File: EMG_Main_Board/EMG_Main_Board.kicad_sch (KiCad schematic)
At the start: 14 parts, among them IC1 EFR32BG13P732F512GM48-D, IC2 LD1117DT18TR, J1 ADC input, J2 USB_C_Receptacle, J3 UART, J4 UART, J5 1.8V, J6 Conn_01x02_Pin, U1 LD1117S33TR_SOT223, U3 STM32G0B1RET6

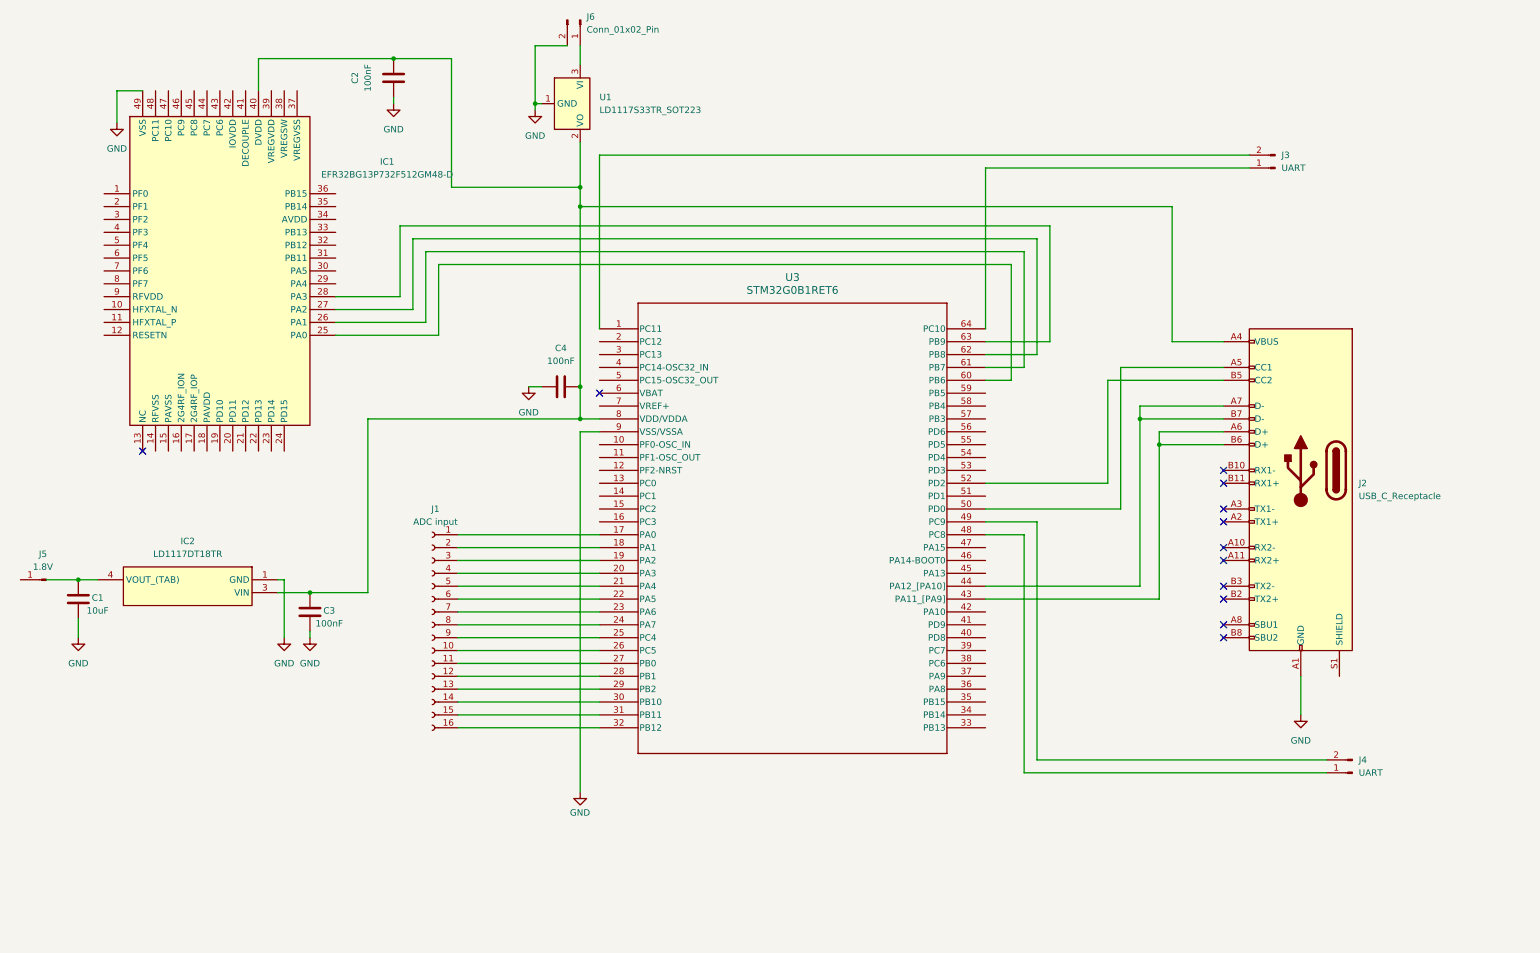
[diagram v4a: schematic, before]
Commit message: add 38.4 and 48MHz crystals for BLE and MCU, resp.
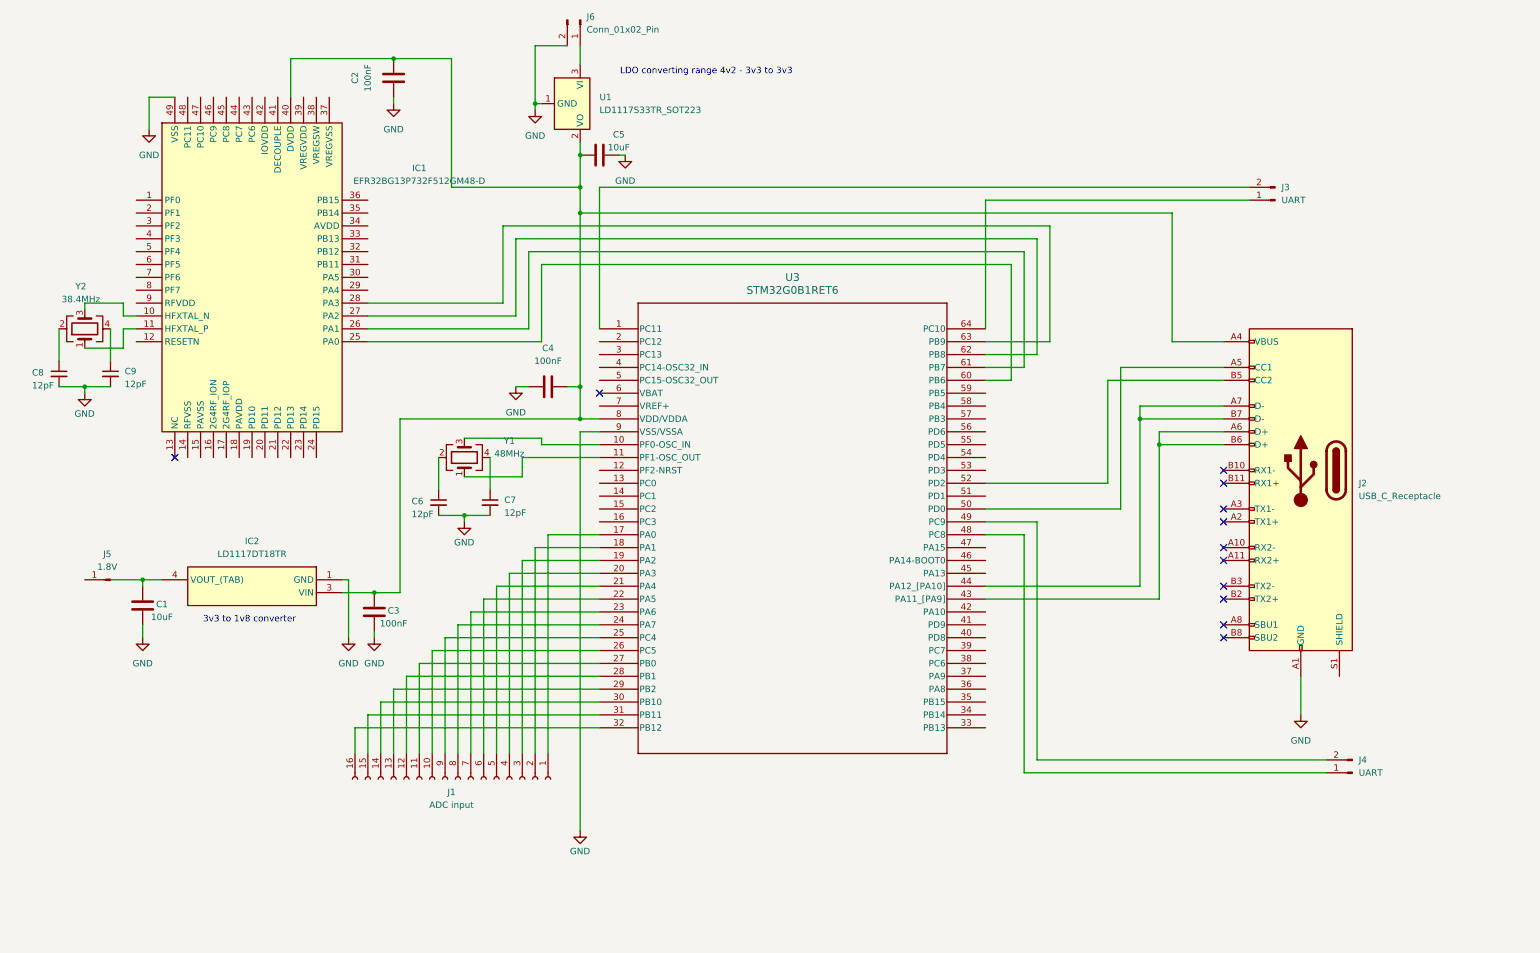
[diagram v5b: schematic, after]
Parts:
- added C5: 10uF, symbol Device:C
- added C6, C7, C8, C9: 12pF, symbol Device:C_Small
- added Y1: 48MHz, symbol Device:Crystal_GND24
- added Y2: 38.4MHz, symbol Device:Crystal_GND24
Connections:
- net GND: now also C5.2, C6.2, C7.2, C8.2, C9.2
- net at C2.1, C3.1, C4.1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: now also C5.1
- net at IC1.10 (HFXTAL_N): now also Y2.3
- net at IC1.11 (HFXTAL_P): now also Y2.1
- net at U3.10 (PF0-OSC_IN): now also Y1.3
- net at U3.11 (PF1-OSC_OUT): now also Y1.1
- new net: C6.1, Y1.2
- new net: C7.1, Y1.4
- new net: C9.1, Y2.4
- new net: C8.1, Y2.2
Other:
- note added: "3v3 to 1v8 converter"
- note added: "LDO converting range 4v2 - 3v3 to 3v3"
- moved on the sheet: C1, C3, C4, IC1, IC2, J1, J3, J5

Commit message: add ON/OFF slide switch and RST button to sch
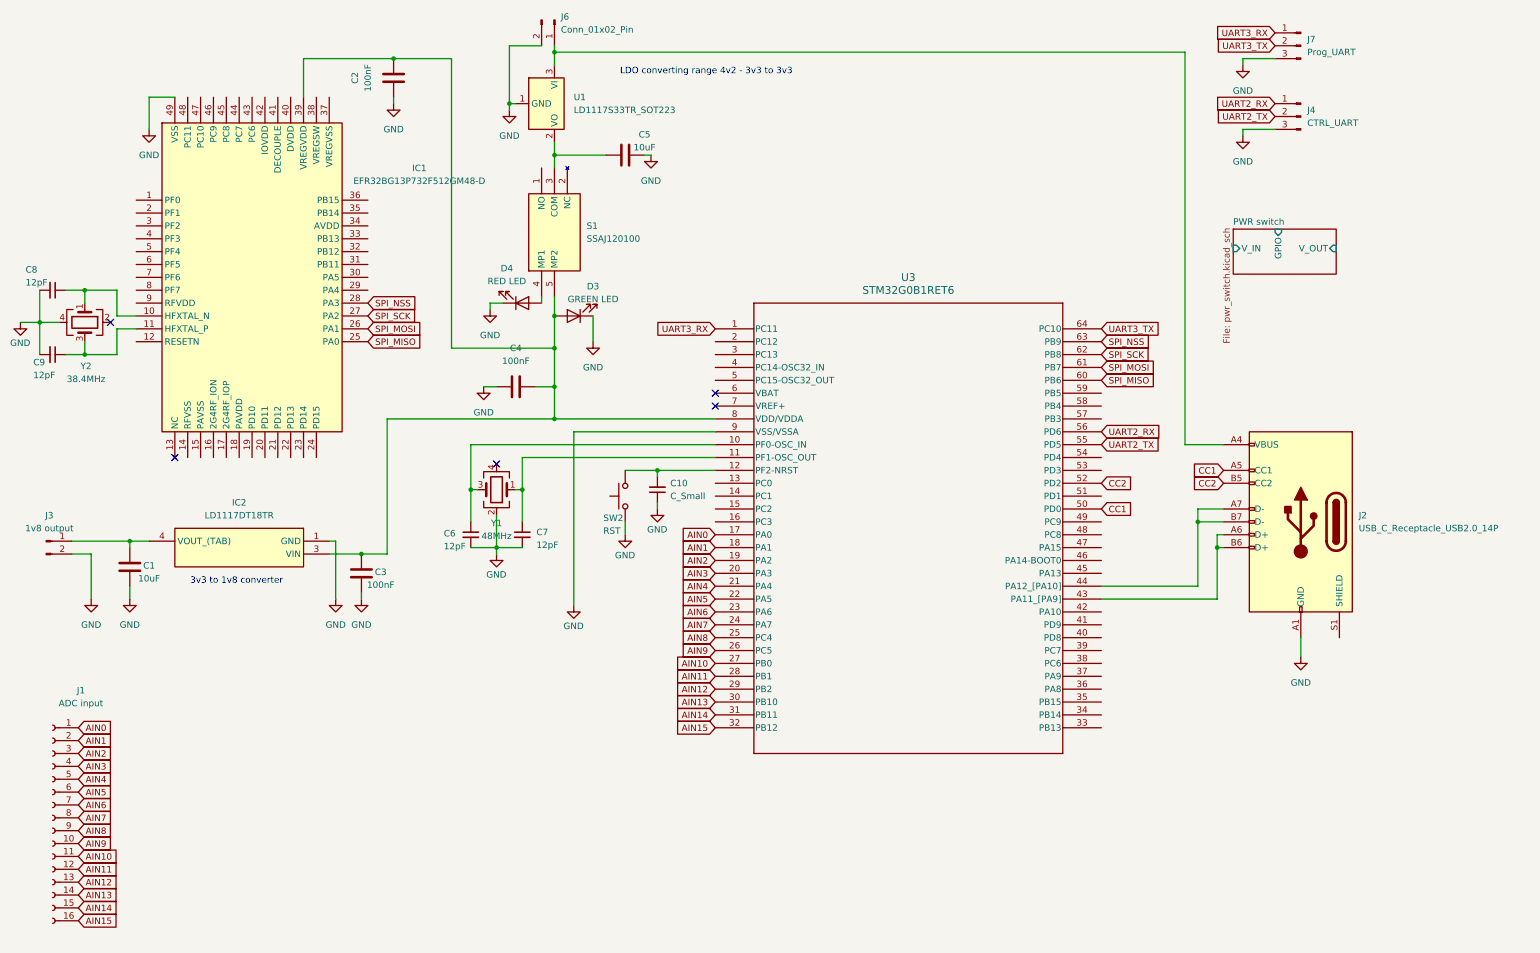
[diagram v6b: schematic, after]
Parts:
- removed J2: USB_C_Receptacle, symbol Connector:USB_C_Receptacle
- removed J4: UART, symbol Connector:Conn_01x02_Pin
- removed J5: 1.8V, symbol Connector:Conn_01x01_Pin
- added C10: C_Small, symbol Device:C_Small
- added D3: GREEN LED, symbol Device:LED
- added D4: RED LED, symbol Device:LED
- added J2: USB_C_Receptacle_USB2.0_14P, symbol Connector:USB_C_Receptacle_USB2.0_14P
- added J4: CTRL_UART, symbol Connector:Conn_01x03_Pin
- added J7: Prog_UART, symbol Connector:Conn_01x03_Pin
- added S1: SSAJ120100, SSAJ120100, symbol SSAJ120100:SSAJ120100
- added SW2: RST, symbol Switch:SW_Push
- J3: value UART -> 1v8 output
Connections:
- net GND: now also J3.2 (Pin_2), Y1.2, Y2.4, C10.1, D3.1 (K), D4.1 (K), J2.A1 (GND), J2.A12 (GND), J2.B1 (GND), J2.B12 (GND), J4.3 (Pin_3), J7.3 (Pin_3), SW2.1
- net at U3.11 (PF1-OSC_OUT), Y1.1: now also C7.1
- net at C6.1: now also U3.10 (PF0-OSC_IN), Y1.3; no longer Y1.2
- net at Y1.4: no longer C7.1
- net at J3.1 (Pin_1): now also C1.1, IC2.4 (VOUT_(TAB)); no longer U3.64 (PC10)
- net UART3_RX: now reaches U3.1 (PC11)
- net UART3_RX: now also J7.1 (Pin_1); no longer J3.2 (Pin_2)
- net at C2.1, C3.1, C4.1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: now also IC1.39 (VREGVDD), D3.2 (A), S1.5 (MP2); no longer C5.1, IC1.40 (DVDD), U1.2 (VO)
- net at J6.1 (Pin_1), U1.3 (VI): now also J2.A4 (VBUS), J2.A9 (VBUS), J2.B4 (VBUS), J2.B9 (VBUS)
- net at IC1.10 (HFXTAL_N): now also C8.1, Y2.1; no longer Y2.3
- net at IC1.11 (HFXTAL_P): now also C9.1, Y2.3; no longer Y2.1
- net SPI_MISO: now reaches IC1.25 (PA0), U3.60 (PB6)
- net SPI_MOSI: now reaches IC1.26 (PA1), U3.61 (PB7)
- net SPI_SCK: now reaches IC1.27 (PA2), U3.62 (PB8)
- net SPI_NSS: now reaches IC1.28 (PA3), U3.63 (PB9)
- net at U3.12 (PF2-NRST): now also C10.2, SW2.2
- net AIN0: now reaches J1.1 (Pin_1), U3.17 (PA0)
- net AIN1: now reaches J1.2 (Pin_2), U3.18 (PA1)
- net AIN2: now reaches J1.3 (Pin_3), U3.19 (PA2)
- net AIN3: now reaches J1.4 (Pin_4), U3.20 (PA3)
- net AIN4: now reaches J1.5 (Pin_5), U3.21 (PA4)
- net AIN5: now reaches J1.6 (Pin_6), U3.22 (PA5)
- net AIN6: now reaches J1.7 (Pin_7), U3.23 (PA6)
- net AIN7: now reaches J1.8 (Pin_8), U3.24 (PA7)
- net AIN8: now reaches J1.9 (Pin_9), U3.25 (PC4)
- net AIN9: now reaches J1.10 (Pin_10), U3.26 (PC5)
- net AIN10: now reaches J1.11 (Pin_11), U3.27 (PB0)
- net AIN11: now reaches J1.12 (Pin_12), U3.28 (PB1)
- net AIN12: now reaches J1.13 (Pin_13), U3.29 (PB2)
- net AIN13: now reaches J1.14 (Pin_14), U3.30 (PB10)
- net AIN14: now reaches J1.15 (Pin_15), U3.31 (PB11)
- net AIN15: now reaches J1.16 (Pin_16), U3.32 (PB12)
- net at U3.43 (PA11_[PA9]): now also J2.A6 (D+), J2.B6 (D+)
- net at U3.44 (PA12_[PA10]): now also J2.A7 (D-), J2.B7 (D-)
- net CC1: now reaches U3.50 (PD0)
- net CC1: now also J2.A5 (CC1)
- net CC2: now reaches U3.52 (PD2)
- net CC2: now also J2.B5 (CC2)
- net UART2_TX: now reaches U3.55 (PD5)
- net UART2_TX: now also J4.2 (Pin_2)
- net UART2_RX: now reaches U3.56 (PD6)
- net UART2_RX: now also J4.1 (Pin_1)
- net at Y2.2: no longer C8.1
- new net: C5.1, S1.3 (COM), U1.2 (VO)
- new net: D4.2 (A), S1.4 (MP1)
- new net UART3_TX: J7.2 (Pin_2), U3.64 (PC10)
- no-connect marks 12 -> 5
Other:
- added sheet PWR switch (pwr_switch.kicad_sch)
- moved on the sheet: C1, C3, C4, C5, C6, C7, C8, C9, IC2, J1, J6, U1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

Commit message: replace slide switch
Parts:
- removed S1: SSAJ120100, SSAJ120100, symbol SSAJ120100:SSAJ120100
- added S1: SC12P-AQR, SC12PAQR, symbol SC12P-AQR:SC12P-AQR
- C10: value C_Small -> 100nF
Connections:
- net at C5.1, U1.2 (VO): now also S1.B1 (B1_COM)
- net at C2.1, C3.1, C4.1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: now also S1.C1 (C1_NO)
- net at D4.2 (A): now also S1.A1 (A1_NC)
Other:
- moved on the sheet: D3, D4

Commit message: add license
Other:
- moved on the sheet: C6, C7, D4, J3, Y1
